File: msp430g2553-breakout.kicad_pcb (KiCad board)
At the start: 2 copper layers, 24 x 42 mm, 26 parts, among them J1 Left, J2 Right, J3 SBW, Q1 BSS138, Q2 BSS138, SW1 Reset, U1 MSP430G2553IPW28, Y1 32.768kHz

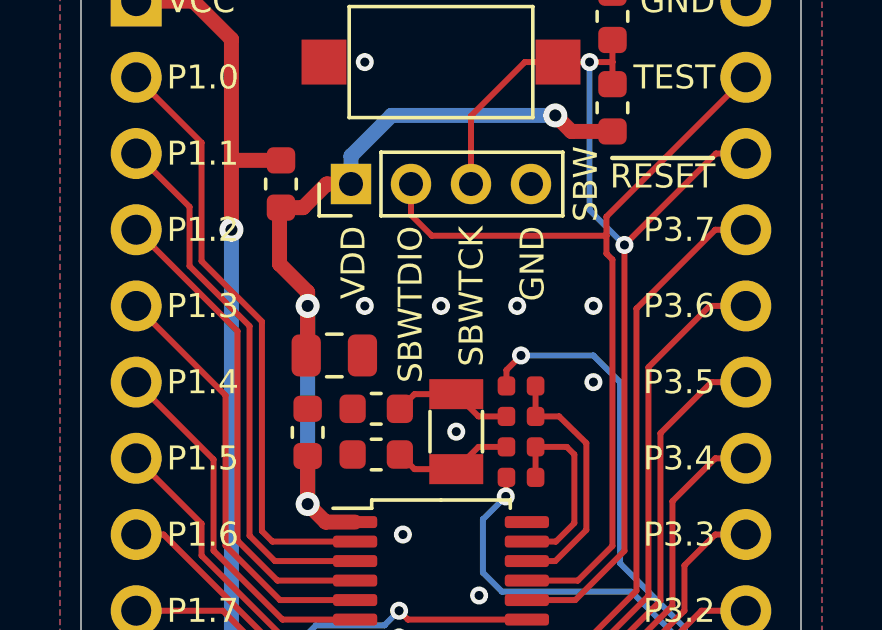
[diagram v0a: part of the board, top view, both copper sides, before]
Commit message: Fixed swapped SBWTDIO and SBWTCK pins, revision bump to A1
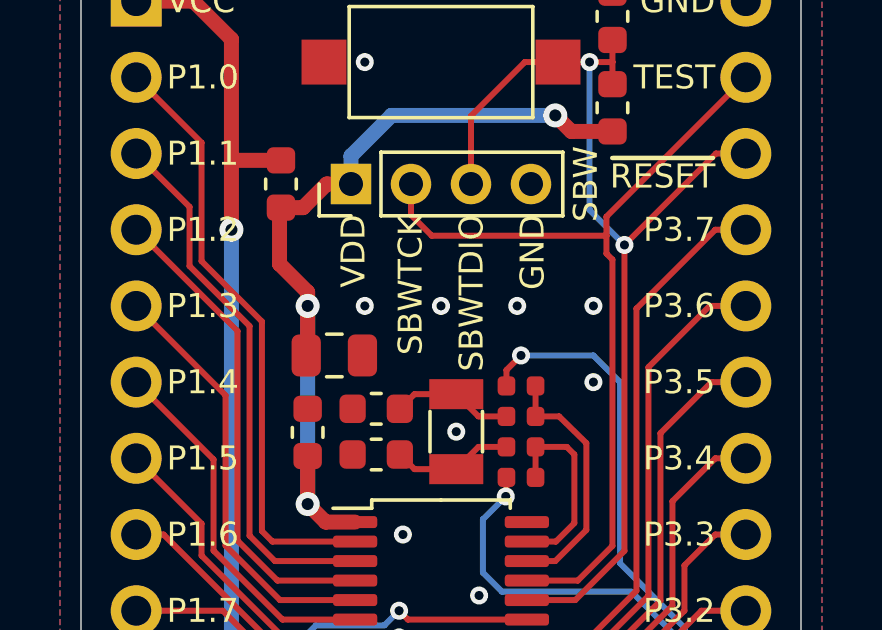
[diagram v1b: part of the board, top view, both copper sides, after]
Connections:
- net /SBWTDIO renamed /TEST
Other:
- board text added: "MSP430G2553 Breakout © 2021 Michal Potrzebicz michal@elevendroids.com CC BY-SA 4.0 Rev. A1"
- board text removed: "MSP430G2553 Breakout © 2020 Michal Potrzebicz michal@elevendroids.com CC BY-SA 4.0 Rev. A"
